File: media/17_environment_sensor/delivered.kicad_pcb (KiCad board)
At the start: 4 copper layers, 50 x 26.5 mm, 107 parts, among them J1 USB-C_GCT_USB4105-GF-A, J2 JST_SH_1x4_SM04B-SRSS-TB-LF-SN, J3 JST_SH_1x4_SM04B-SRSS-TB-LF-SN, U1 FT232R_QFN, U2 AP7370-33SA-7, U3 STM32G474CET6, U4 MB85RC1MTPNF-G, U5 SHT45, U6 BME280, Y1 Resonator_32.768kHz_ECX-31B, Y2 Resonator_8MHz_ABM3B

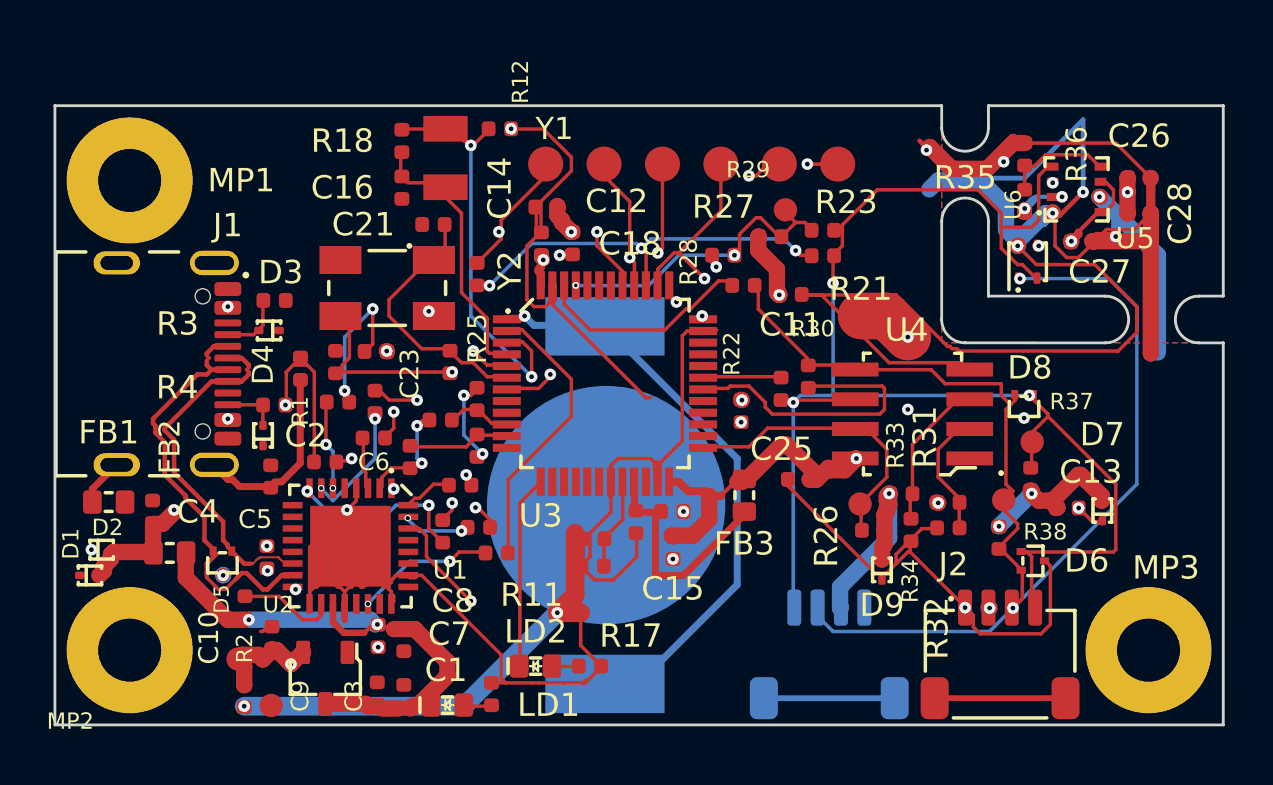
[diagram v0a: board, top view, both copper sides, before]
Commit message: gpm: environment_sensor re-run (mounting holes declared), audits, follow-up issues #1442-#1444
Co-Authored-By: Claude Opus 5.5 <noreply@anthropic.com>
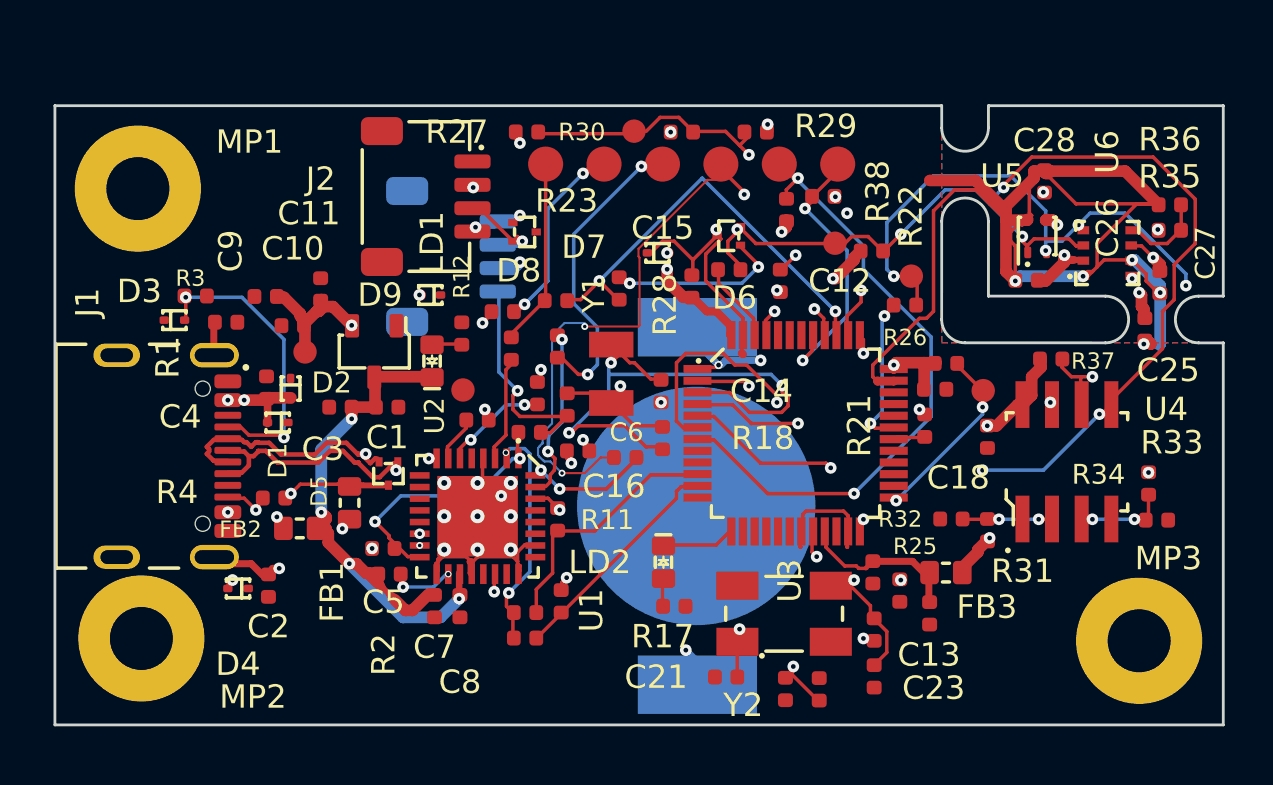
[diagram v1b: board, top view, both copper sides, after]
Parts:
- moved J2 31.6 mm to (175.7, 117.4), turned to -90 degrees
- moved C23 26.7 mm to (195.1, 137.9), turned to 90 degrees
- moved J3 23.7 mm to (176.8, 120.0), turned to 90 degrees
- moved C21 23.1 mm to (188.7, 138.0)
- moved D8 22.6 mm to (180.1, 118.9), turned to 0 degrees
- moved D9 22.6 mm to (176.1, 121.6), turned to 180 degrees
- moved D7 22.0 mm to (185.8, 119.8), turned to 0 degrees
- moved Y2 22.0 mm to (191.2, 135.2), turned to 90 degrees
- moved R25 21.5 mm to (195.1, 135.9), turned to 90 degrees
- moved C18 20.8 mm to (199.9, 127.7), turned to 90 degrees
- moved R24 20.3 mm to (192.9, 117.4)
- moved C11 20.1 mm to (171.4, 121.4), turned to 90 degrees
- moved D6 19.0 mm to (188.8, 119.1), turned to 180 degrees
- moved C9 17.1 mm to (169.0, 121.7), turned to 0 degrees
- moved R18 16.9 mm to (186.0, 127.7), turned to 90 degrees
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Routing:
- net GND: track 233.0 -> 109.8 mm, vias 26 -> 22
- net NRST: track 28.3 -> 45.5 mm, vias 4 -> 3
- net Net-(U3-PF1-OSC_OUT): track 10.2 -> 26.2 mm, vias 0 -> 3
- net Net-(U1-TXD): track 16.0 -> 4.67 mm, vias 3 -> 2
- net Net-(U3-PA8): track 12.5 -> 1.20 mm
- net SWCLK-JTCK: track 22.8 -> 33.0 mm, vias 2 -> 5
- net /USB_CC1: track 2.77 -> 12.1 mm, vias 0 -> 2
- net JTDI: track 15.7 -> 7.78 mm, vias 2 -> 0
- net JTRST: track 32.0 -> 24.1 mm, vias 4 -> 3
- net LPUART_1_STM_TX: track 2.76 -> 10.6 mm
- net /OSC32_OUT: track 10.7 -> 17.5 mm, vias 0 -> 2
- net /OSC32_IN: track 17.5 -> 24.1 mm, vias 2 -> 3
- net Net-(U3-PF0-OSC_IN): track 9.65 -> 16.2 mm
- net I2C_1_SCL: track 62.1 -> 55.5 mm, vias 3 -> 10
- net GNDREF: track 30.0 -> 23.8 mm, vias 0 -> 2
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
